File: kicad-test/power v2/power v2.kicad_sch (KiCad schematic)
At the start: 0 parts

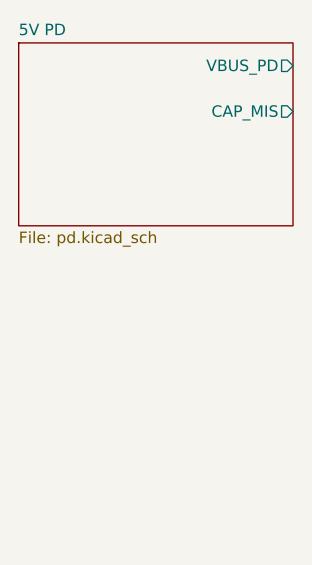
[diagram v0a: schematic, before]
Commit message: usb device connection
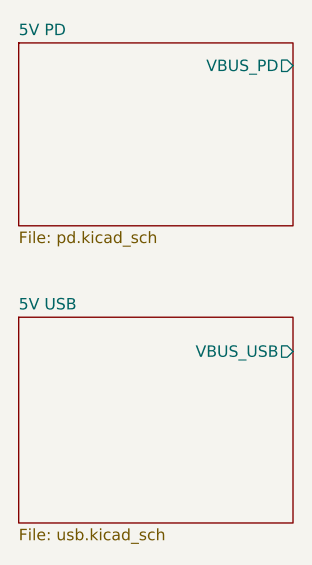
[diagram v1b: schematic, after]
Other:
- added sheet 5V USB (usb.kicad_sch)
- sheet 5V PD ports: added none; removed CAP_MIS
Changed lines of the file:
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@@
+	)
+	(sheet
+		(at 50.8 78.74)
+		(size 30.48 22.86)
+		(exclude_from_sim no)
+		(in_bom yes)
+		(on_board yes)
+		(dnp no)
+		(fields_autoplaced yes)
+		(stroke
+			(width 0.1524)
+			(type solid)
+		)
+		(fill
+			(color 0 0 0 0)
+		)
+		(property "Sheetname" "5V USB"
+			(at 50.8 78.0284 0)
+			(show_name no)
+			(do_not_autoplace no)
+			(effects
+				(font
+					(size 1.27 1.27)
+				)
+				(justify left bottom)
+			)
+		)
+		(property "Sheetfile" "usb.kicad_sch"
+			(at 50.8 102.1846 0)
+			(show_name no)
+			(do_not_autoplace no)
+			(effects
+				(font
+					(size 1.27 1.27)
+				)
+				(justify left top)
+			)
+		)
+		(pin "VBUS_USB" output
+			(at 81.28 82.55 0)
+			(effects
+				(font
+					(size 1.27 1.27)
+				)
+				(justify right)
+			)
+		)
+		(instances
+			(project "power v2"
+				(path "/7765ea03-990c-41e2-8b83-b7e84578cc41"
+					(page "3")
+				)
+			)
+		)
 	)
 	(sheet
@@
 			)
 		)
-		(pin "CAP_MIS" output
-			(at 81.28 55.88 0)
-			(effects
-				(font
-					(size 1.27 1.27)
-				)
-				(justify right)
-			)
-		)

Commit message: add footprints
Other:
- added sheet Input Selector (select.kicad_sch)
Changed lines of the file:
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@@
 		(title "Power test board v0.2")
+	)
+	(wire
+		(pts
+			(xy 102.87 69.85) (xy 88.9 69.85)
+		)
+		(stroke
+			(width 0)
+			(type default)
+		)
+	)
+	(wire
+		(pts
+			(xy 129.54 69.85) (xy 133.35 69.85)
+		)
+		(stroke
+			(width 0)
+			(type default)
+		)
+	)
+	(wire
+		(pts
+			(xy 88.9 50.8) (xy 81.28 50.8)
+		)
+		(stroke
+			(width 0)
+			(type default)
+		)
+	)
+	(wire
+		(pts
+			(xy 88.9 82.55) (xy 88.9 76.2)
+		)
+		(stroke
+			(width 0)
+			(type default)
+		)
+	)
+	(wire
+		(pts
+			(xy 88.9 76.2) (xy 102.87 76.2)
+		)
+		(stroke
+			(width 0)
+			(type default)
+		)
+	)
+	(wire
+		(pts
+			(xy 81.28 82.55) (xy 88.9 82.55)
+		)
+		(stroke
+			(width 0)
+			(type default)
+		)
+	)
+	(wire
+		(pts
+			(xy 88.9 69.85) (xy 88.9 50.8)
+		)
+		(stroke
+			(width 0)
+			(type default)
+		)
+	)
+	(symbol
+		(lib_id "power:+5V")
+		(at 133.35 69.85 0)
+		(unit 1)
+		(body_style 1)
+		(exclude_from_sim no)
+		(in_bom yes)
+		(on_board yes)
+		(in_pos_files yes)
+		(dnp no)
+		(fields_autoplaced yes)
+		(property "Reference" "#PWR028"
+			(at 133.35 73.66 0)
+			(hide yes)
+			(show_name no)
+			(do_not_autoplace no)
+			(effects
+				(font
+					(size 1.27 1.27)
+				)
+			)
+		)
+		(property "Value" "+5V"
+			(at 133.35 64.77 0)
+			(show_name no)
+			(do_not_autoplace no)
+			(effects
+				(font
+					(size 1.27 1.27)
+				)
+			)
+		)
+		(property "Footprint" ""
+			(at 133.35 69.85 0)
+			(hide yes)
+			(show_name no)
+			(do_not_autoplace no)
+			(effects
+				(font
+					(size 1.27 1.27)
+				)
+			)
+		)
+		(property "Datasheet" ""
+			(at 133.35 69.85 0)
+			(hide yes)
+			(show_name no)
+			(do_not_autoplace no)
+			(effects
+				(font
+					(size 1.27 1.27)
+				)
+			)
+		)
+		(property "Description" "Power symbol creates a global label with name \"+5V\""
+			(at 133.35 69.85 0)
+			(hide yes)
+			(show_name no)
+			(do_not_autoplace no)
+			(effects
+				(font
+					(size 1.27 1.27)
+				)
+			)
+		)
+		(pin "1"
+		)
+		(instances
+			(project "power v2"
+				(path "/7765ea03-990c-41e2-8b83-b7e84578cc41"
+					(reference "#PWR028")
+					(unit 1)
+				)
+			)
+		)
+	)
+	(sheet
+		(at 102.87 66.04)
+		(size 26.67 17.78)
+		(exclude_from_sim no)
+		(in_bom yes)
+		(on_board yes)
+		(dnp no)
+		(fields_autoplaced yes)
+		(stroke
+			(width 0.1524)
+			(type solid)
+		)
+		(fill
+			(color 0 0 0 0)
+		)
+		(property "Sheetname" "Input Selector"
+			(at 102.87 65.3284 0)
+			(show_name no)
+			(do_not_autoplace no)
+			(effects
+				(font
+					(size 1.27 1.27)
+				)
+				(justify left bottom)
+			)
+		)
+		(property "Sheetfile" "select.kicad_sch"
+			(at 102.87 84.4046 0)
+			(show_name no)
+			(do_not_autoplace no)
+			(effects
+				(font
+					(size 1.27 1.27)
+				)
+				(justify left top)
+			)
+		)
+		(pin "VBUS_PD" input
+			(at 102.87 69.85 180)
+			(effects
+				(font
+					(size 1.27 1.27)
+				)
+				(justify left)
+			)
+		)
+		(pin "VBUS_USB" input
+			(at 102.87 76.2 180)
+			(effects
+				(font
+					(size 1.27 1.27)
+				)
+				(justify left)
+			)
+		)
+		(pin "VOUT" output
+			(at 129.54 69.85 0)
+			(effects
+				(font
+					(size 1.27 1.27)
+				)
+				(justify right)
+			)
+		)
+		(instances
+			(project "power v2"
+				(path "/7765ea03-990c-41e2-8b83-b7e84578cc41"
+					(page "4")
+				)
+			)
+		)
 	)
 	(sheet

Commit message: pcb layout
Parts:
- added D1: R, LED_SMD:LED_0805_2012Metric_Pad1.15x1.40mm_HandSolder, symbol Device:LED_Small
- added J1: 5V OUT, Connector_PinHeader_2.54mm:PinHeader_1x02_P2.54mm_Vertical, symbol Connector:Conn_01x02_Pin
- added R1: 1k, Resistor_SMD:R_0805_2012Metric_Pad1.20x1.40mm_HandSolder, symbol Device:R_Small_US
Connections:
- net +5V: now also D1.2 (A), J1.2 (Pin_2)
- new net: D1.1 (K), R1.1
- new net GND: J1.1 (Pin_1), R1.2
